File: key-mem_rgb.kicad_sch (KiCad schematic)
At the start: 4 parts

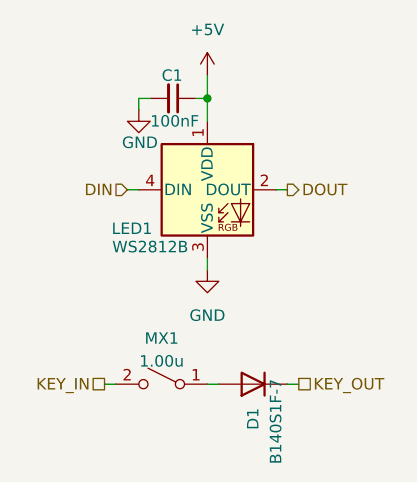
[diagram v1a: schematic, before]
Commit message: Switch to matrix RGB LED
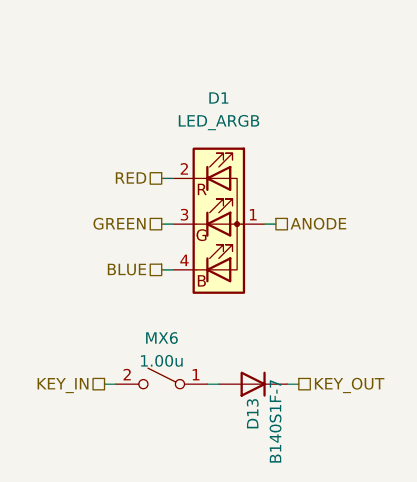
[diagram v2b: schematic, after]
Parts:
- removed C1: 100nF, keyboard:C_0402_1005Metric, symbol Device:C_Small
- removed LED1: WS2812B, keyboard:LED_WS2812B-2020_PLCC4_2.0x2.0mm, symbol keyboard:WS2812B
- added D1: LED_ARGB, symbol Device:LED_ARGB
- renumbered D1 to D13, MX1 to MX6
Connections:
- new net ANODE: D1.1 (A)
- new net BLUE: D1.4 (BK)
- new net GREEN: D1.3 (GK)
- new net RED: D1.2 (RK)
